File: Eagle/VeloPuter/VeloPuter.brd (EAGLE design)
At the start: 99.1 x 61 mm, 36 parts

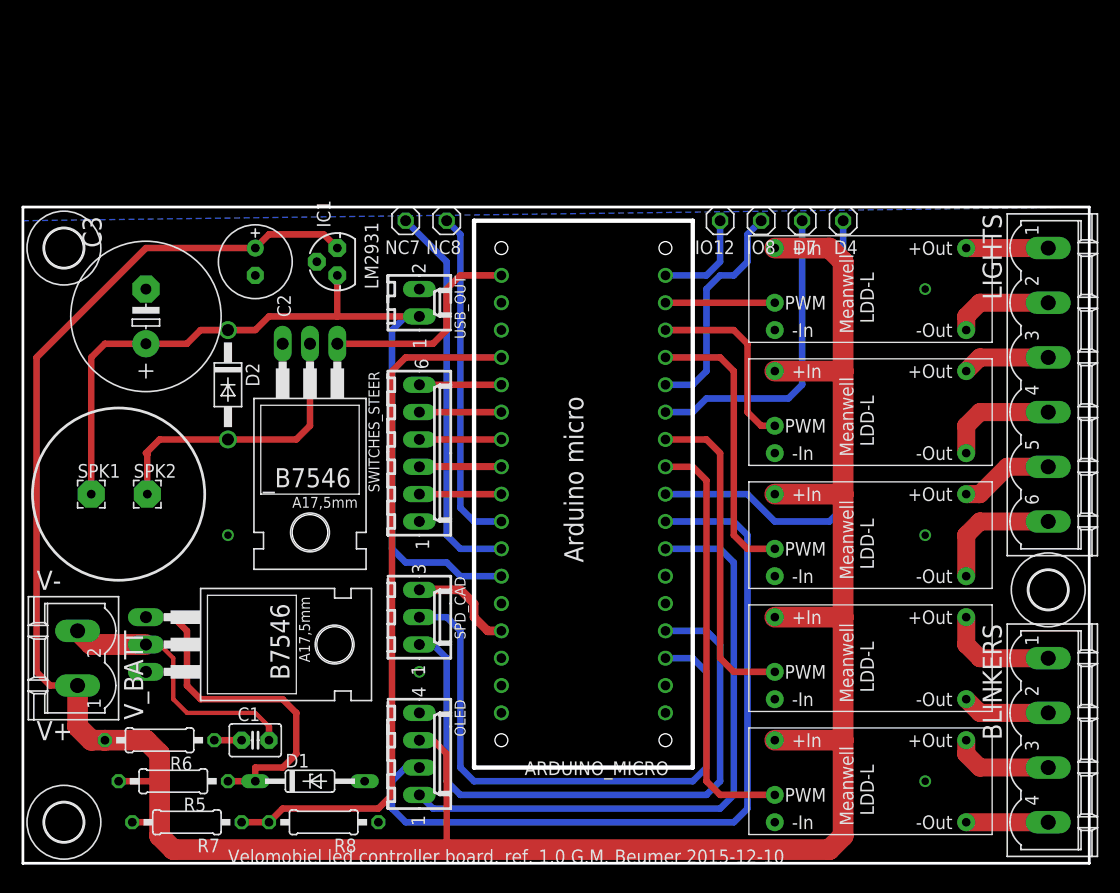
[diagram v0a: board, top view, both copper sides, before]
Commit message: Partial redesign due to insights from the first builds - VDD of the oled now goes to the 5V not Vbatt. - Larger capacitor for C2. - LM2931 replaced by a TO220 (need new layout for this) - Brake handle now goes to pin nr 7 because that is a pin with an interupt. - reorganised the free pins. - Allowed for some wirering below the arduinio itself (for now just the extra pins which are used) -
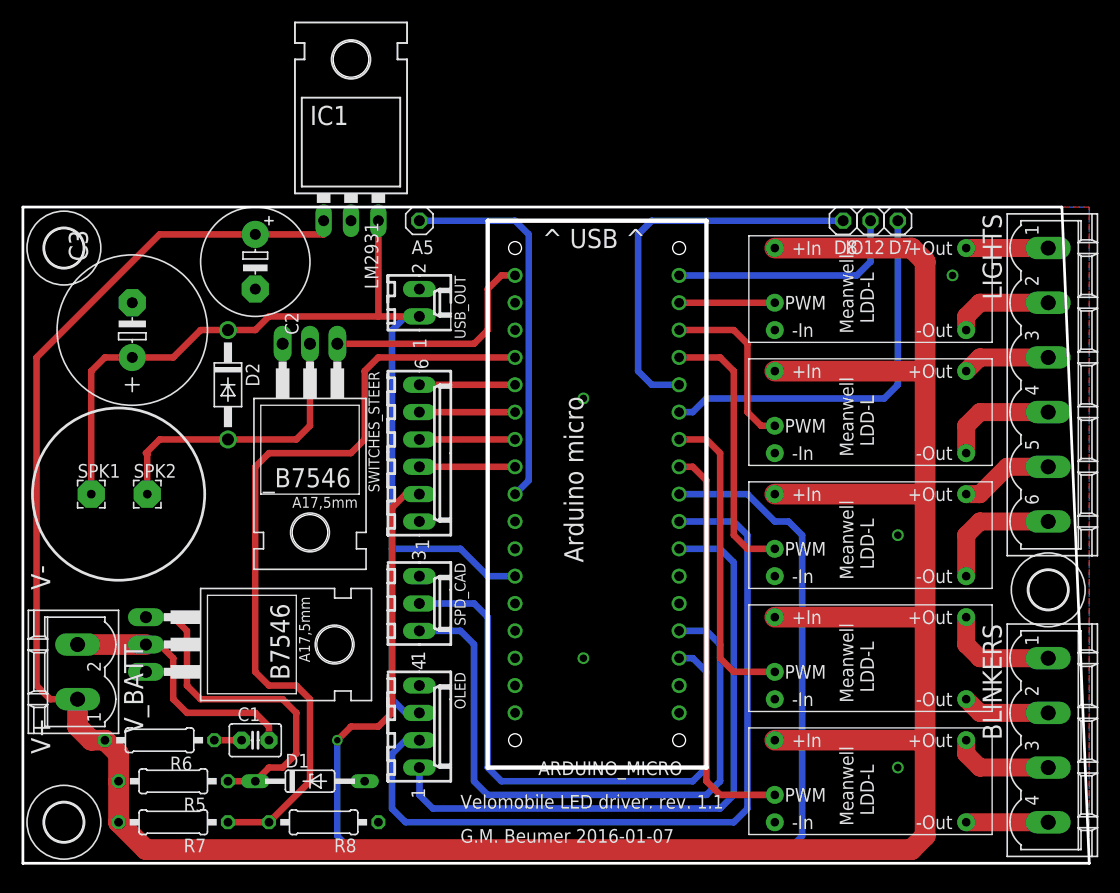
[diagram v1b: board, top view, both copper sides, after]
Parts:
- removed IO8, NC7, NC8: (no value), pinhead:1X01
- added A5: A5, pinhead:1X01
- C2: device rcl:E2,5-7 -> rcl:E5-10,5
- IC1: value (none) -> LM2931T-L; device v-reg-3:TO92 -> v-reg-3:TO220L1
- moved IO12 14.0 mm to (82.5, 80.0)
- moved D7 8.89 mm to (85.1, 80.0)
- moved IC1 7.73 mm to (34.3, 83.8), turned to 0 degrees
- moved OLED 2.54 mm to (40.6, 33.0)
- moved C3 1.80 mm to (14.0, 69.8)
- moved ARDUINO_MICRO 1.27 mm to (66.0, 76.2)
- moved SPD_CAD 1.27 mm to (40.6, 44.5)
- moved R7 1.27 mm to (17.8, 24.1)
- moved V_BATT 1.27 mm to (8.89, 38.1)
- renumbered D4 to D8
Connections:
- removed net N$15: ARDUINO_MICRO.D4, D8.1
- removed net N$19: ARDUINO_MICRO.NC8, NC8.1
- removed net N$20: ARDUINO_MICRO.NC7, NC7.1
- new net A5: A5.1, ARDUINO_MICRO.A5
- net 5V: now also IC1.3, OLED.3; no longer IC1.1
- net BRAKE_SWITCH: now also ARDUINO_MICRO.D4; no longer ARDUINO_MICRO.A5
- net N$17: now also D8.1; no longer IO8.1
- net V+: now also IC1.1; no longer IC1.3, OLED.3
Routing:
- net BRAKE_SWITCH: track 7.62 -> 122.3 mm, vias 0 -> 1
- net N$15: track 44.8 -> 0.00 mm
- net N$20: track 36.4 -> 0.00 mm
- net A5: track 0.00 -> 35.3 mm
- net N$19: track 31.5 -> 0.00 mm
- net V+: track 255.3 -> 281.5 mm
- net 5V: track 83.2 -> 105.8 mm
- net N$17: track 21.2 -> 36.6 mm
- net IO12: track 9.42 -> 22.1 mm
- net GND: track 9.94 -> 0.00 mm
- net V_0: track 65.1 -> 74.1 mm
- net N$16: track 29.0 -> 36.6 mm
- net UP_SWITCH: track 15.2 -> 8.89 mm
- net SCL_OLED: track 73.2 -> 74.5 mm
- net PWM_BUZZER: track 20.1 -> 21.4 mm
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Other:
- outline, holes or cut-outs redrawn
- board text added: "G.M. Beumer 2016-01-07"
- board text added: "Velomobile LED driver. rev. 1.1"
- board text added: "^ USB ^"
- board text removed: "Velomobiel led controller board. ref. 1.0 G.M. Beumer 2015-12-10"

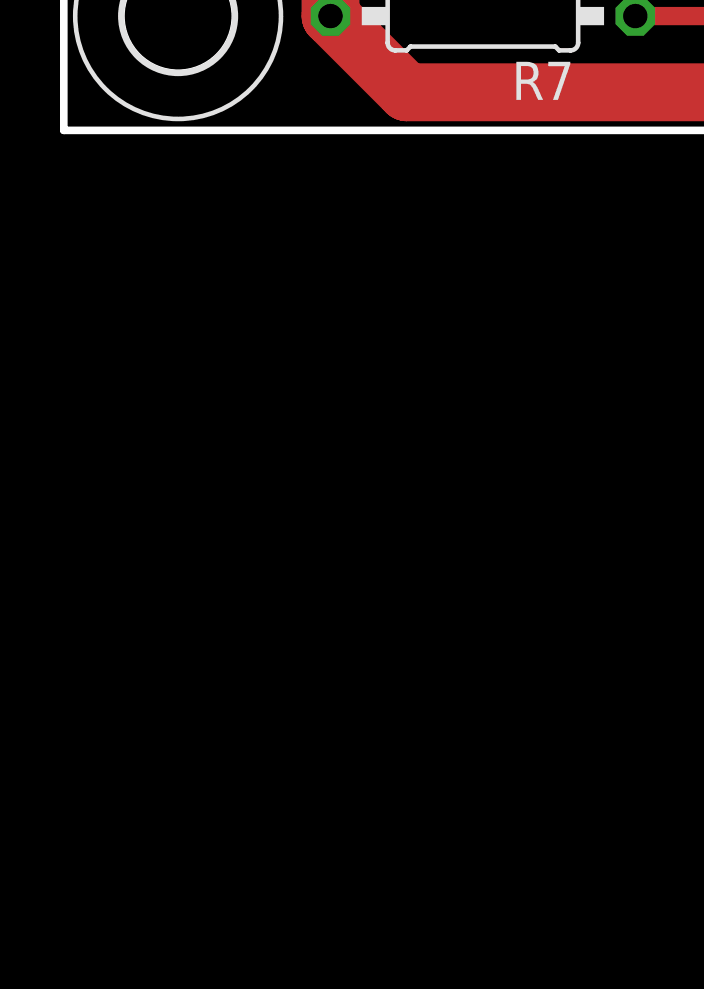
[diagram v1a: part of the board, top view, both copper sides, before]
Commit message: Added pulldown resistors for the LDD700 PWM inputs. Without these resistors the LED's would flash brightly before the arduino kicks in.
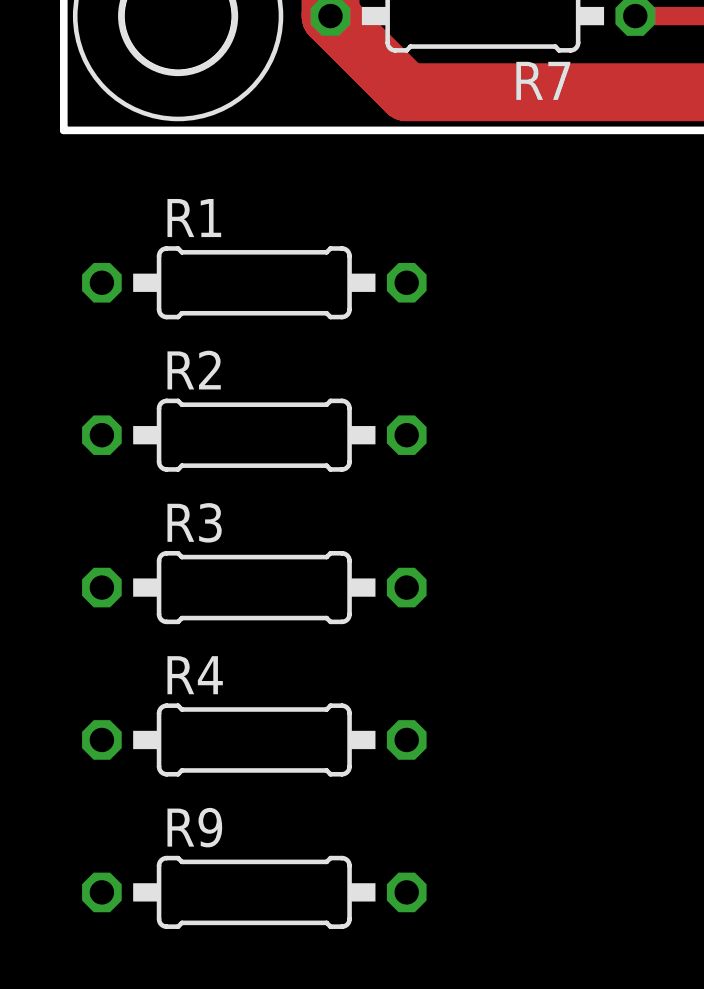
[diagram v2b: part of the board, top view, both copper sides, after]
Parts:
- added R1, R2, R3, R4: 100k, resistor:0207/10
- added R9: 100l, resistor:0207/10
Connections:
- net GND: now also R1.1, R2.1, R3.1, R4.1, R9.1
- net PWM_BRAKE: now also R1.2
- net PWM_FRONT1: now also R4.2
- net PWM_FRONT2: now also R9.2
- net PWM_LEFT: now also R2.2
- net PWM_RIGHT: now also R3.2
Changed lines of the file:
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@@
 <attribute name="MPN" value="" x="85.09" y="80.01" size="1.778" layer="27" rot="R180" display="off"/>
+</element>
+<element name="R1" library="resistor" package="0207/10" value="100k" x="10.16" y="15.24">
+<attribute name="OC_NEWARK" value="unknown" x="10.16" y="15.24" size="1.778" layer="27" display="off"/>
+<attribute name="MPN" value="" x="10.16" y="15.24" size="1.778" layer="27" display="off"/>
+<attribute name="MF" value="" x="10.16" y="15.24" size="1.778" layer="27" display="off"/>
+</element>
+<element name="R2" library="resistor" package="0207/10" value="100k" x="10.16" y="10.16">
+<attribute name="OC_NEWARK" value="unknown" x="10.16" y="10.16" size="1.778" layer="27" display="off"/>
+<attribute name="MPN" value="" x="10.16" y="10.16" size="1.778" layer="27" display="off"/>
+<attribute name="MF" value="" x="10.16" y="10.16" size="1.778" layer="27" display="off"/>
+</element>
+<element name="R3" library="resistor" package="0207/10" value="100k" x="10.16" y="5.08">
+<attribute name="OC_NEWARK" value="unknown" x="10.16" y="5.08" size="1.778" layer="27" display="off"/>
+<attribute name="MPN" value="" x="10.16" y="5.08" size="1.778" layer="27" display="off"/>
+<attribute name="MF" value="" x="10.16" y="5.08" size="1.778" layer="27" display="off"/>
+</element>
+<element name="R4" library="resistor" package="0207/10" value="100k" x="10.16" y="0">
+<attribute name="OC_NEWARK" value="unknown" x="10.16" y="0" size="1.778" layer="27" display="off"/>
+<attribute name="MPN" value="" x="10.16" y="0" size="1.778" layer="27" display="off"/>
+<attribute name="MF" value="" x="10.16" y="0" size="1.778" layer="27" display="off"/>
+</element>
+<element name="R9" library="resistor" package="0207/10" value="100l" x="10.16" y="-5.08">
+<attribute name="OC_NEWARK" value="unknown" x="10.16" y="-5.08" size="1.778" layer="27" display="off"/>
+<attribute name="MPN" value="" x="10.16" y="-5.08" size="1.778" layer="27" display="off"/>
+<attribute name="MF" value="" x="10.16" y="-5.08" size="1.778" layer="27" display="off"/>
 </element>
 </elements>
@@
 <via x="55.88" y="63.5" extent="1-16" drill="0.7" shape="square"/>
 <via x="55.88" y="39.37" extent="1-16" drill="0.7" shape="square"/>
-<wire x1="73.66" y1="46.99" x2="64.77" y2="46.99" width="0" layer="19" extent="1-1"/>
+<contactref element="R1" pad="1"/>
+<contactref element="R2" pad="1"/>
+<contactref element="R3" pad="1"/>
+<contactref element="R4" pad="1"/>
+<contactref element="R9" pad="1"/>
+<wire x1="73.66" y1="69.85" x2="90.17" y2="74.93" width="0" layer="19" extent="1-1"/>
+<wire x1="73.66" y1="58.42" x2="73.66" y2="69.85" width="0" layer="19" extent="1-1"/>
+<wire x1="73.66" y1="46.99" x2="73.66" y2="58.42" width="0" layer="19" extent="1-1"/>
+<wire x1="64.77" y1="46.99" x2="73.66" y2="46.99" width="0" layer="19" extent="1-1"/>
+<wire x1="73.66" y1="35.56" x2="73.66" y2="46.99" width="0" layer="19" extent="1-1"/>
+<wire x1="73.66" y1="24.13" x2="73.66" y2="35.56" width="0" layer="19" extent="1-1"/>
+<wire x1="55.88" y1="39.37" x2="64.77" y2="46.99" width="0" layer="19" extent="1-1"/>
+<wire x1="49.53" y1="41.91" x2="55.88" y2="39.37" width="0" layer="19" extent="1-1"/>
+<wire x1="40.64" y1="46.99" x2="49.53" y2="41.91" width="0" layer="19" extent="1-1"/>
+<wire x1="40.64" y1="52.07" x2="40.64" y2="46.99" width="0" layer="19" extent="1-1"/>
+<wire x1="40.64" y1="36.83" x2="40.64" y2="46.99" width="0" layer="19" extent="1-1"/>
+<wire x1="35.56" y1="27.94" x2="40.64" y2="36.83" width="0" layer="19" extent="1-1"/>
+<wire x1="36.83" y1="24.13" x2="35.56" y2="27.94" width="0" layer="19" extent="1-1"/>
+<wire x1="85.09" y1="50.8" x2="73.66" y2="46.99" width="0" layer="19" extent="1-1"/>
+<wire x1="85.09" y1="29.21" x2="73.66" y2="24.13" width="0" layer="19" extent="1-1"/>
+<wire x1="55.88" y1="63.5" x2="73.66" y2="58.42" width="0" layer="19" extent="1-1"/>
+<wire x1="40.64" y1="73.66" x2="55.88" y2="63.5" width="0" layer="19" extent="1-1"/>
+<wire x1="34.29" y1="80.01" x2="40.64" y2="73.66" width="0" layer="19" extent="1-1"/>
+<wire x1="25.4" y1="73.66" x2="34.29" y2="80.01" width="0" layer="19" extent="1-1"/>
+<wire x1="27.94" y1="68.58" x2="25.4" y2="73.66" width="0" layer="19" extent="1-1"/>
+<wire x1="13.97" y1="72.39" x2="25.4" y2="73.66" width="0" layer="19" extent="1-1"/>
+<wire x1="15.24" y1="38.1" x2="35.56" y2="27.94" width="0" layer="19" extent="1-1"/>
+<wire x1="5.08" y1="15.24" x2="15.24" y2="38.1" width="0" layer="19" extent="1-1"/>
+<wire x1="5.08" y1="10.16" x2="5.08" y2="15.24" width="0" layer="19" extent="1-1"/>
+<wire x1="5.08" y1="5.08" x2="5.08" y2="10.16" width="0" layer="19" extent="1-1"/>
+<wire x1="5.08" y1="0" x2="5.08" y2="5.08" width="0" layer="19" extent="1-1"/>
+<wire x1="5.08" y1="-5.08" x2="5.08" y2="0" width="0" layer="19" extent="1-1"/>
 </signal>
 <signal name="V+">
@@
 <wire x1="68.58" y1="67.31" x2="69.85" y2="66.04" width="0.6096" layer="1"/>
 <wire x1="69.85" y1="66.04" x2="69.85" y2="50.8" width="0.6096" layer="1"/>
+<contactref element="R1" pad="2"/>
+<wire x1="15.24" y1="15.24" x2="69.85" y2="50.8" width="0" layer="19" extent="1-1"/>
 </signal>
 <signal name="WHEEL_SWITCH">
@@
 <wire x1="68.58" y1="58.42" x2="67.31" y2="59.69" width="0.6096" layer="1"/>
 <wire x1="67.31" y1="59.69" x2="64.77" y2="59.69" width="0.6096" layer="1"/>
+<contactref element="R2" pad="2"/>
+<wire x1="15.24" y1="10.16" x2="68.58" y2="39.37" width="0" layer="19" extent="1-1"/>
 </signal>
 <signal name="PWM_RIGHT">
@@
 <wire x1="67.31" y1="27.94" x2="68.58" y2="26.67" width="0.6096" layer="1"/>
 <wire x1="68.58" y1="26.67" x2="73.66" y2="26.67" width="0.6096" layer="1"/>
+<contactref element="R3" pad="2"/>
+<wire x1="15.24" y1="5.08" x2="67.31" y2="27.94" width="0" layer="19" extent="1-1"/>
 </signal>
 <signal name="PWM_FRONT1">
@@
 <contactref element="ARDUINO_MICRO" pad="D11"/>
 <wire x1="73.66" y1="72.39" x2="64.77" y2="72.39" width="0.6096" layer="1"/>
+<contactref element="R4" pad="2"/>
+<wire x1="15.24" y1="0" x2="64.77" y2="72.39" width="0" layer="19" extent="1-1"/>
 </signal>
 <signal name="PWM_FRONT2">
@@
 <wire x1="69.85" y1="69.85" x2="71.12" y2="68.58" width="0.6096" layer="1"/>
 <wire x1="71.12" y1="68.58" x2="71.12" y2="62.23" width="0.6096" layer="1"/>
+<contactref element="R9" pad="2"/>
+<wire x1="15.24" y1="-5.08" x2="72.39" y2="60.96" width="0" layer="19" extent="1-1"/>
 </signal>
 <signal name="UP_SWITCH">
